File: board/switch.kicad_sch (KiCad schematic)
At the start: 2 parts

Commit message: Fix PCB problems
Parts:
- renumbered D_L_4_0 to D_L_4_2, SW_L_4_0 to SW_L_4_2
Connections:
- net ROW: now also D_L_4_2.1 (K); no longer D_L_4_2.2 (A)
- net at SW_L_4_2.5: now also D_L_4_2.2 (A); no longer D_L_4_2.1 (K)
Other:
- moved on the sheet: D_L_4_2

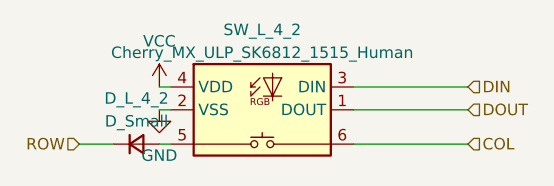
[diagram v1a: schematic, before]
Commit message: Switched to SMD switches
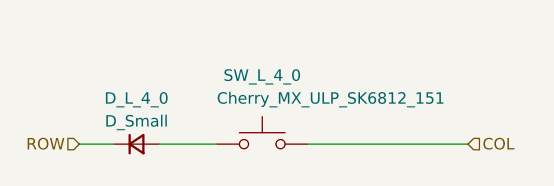
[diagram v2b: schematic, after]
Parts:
- D_L_4_0: renamed from D_L_4_2; LCSC (none) -> C2099
- SW_L_4_0: renamed from SW_L_4_2; value Cherry_MX_ULP_SK6812_1515_Human -> Cherry_MX_ULP_SK6812_151; footprint mnhttn:Cherry_MX_ULP_Human -> mnhttn:Cherry_MX_ULP; symbol mnhttn:Cherry_MX_ULP_SK6812_1515_Human -> Switch:SW_Push
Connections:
- net DOUT is gone; now on an unnamed net: SW_L_4_0.1
- net GND is gone; now on net COL: SW_L_4_0.2
- net COL: no longer SW_L_4_0.6
- net at D_L_4_0.2 (A): no longer SW_L_4_0.5
- removed net DIN: SW_L_4_0.3 (DIN)
- removed net VCC: SW_L_4_0.4 (VDD)

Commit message: Add battery connector
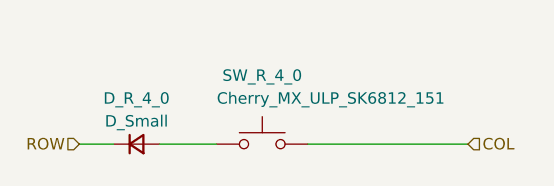
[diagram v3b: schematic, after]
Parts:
- renumbered D_L_4_0 to D_R_4_0, SW_L_4_0 to SW_R_4_0
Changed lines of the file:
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@@
 (kicad_sch
-	(version 20231120)
+	(version 20250114)
 	(generator "eeschema")
-	(generator_version "8.0")
+	(generator_version "9.0")
 	(paper "A4")
 	(wire
@@
 		(shape input)
 		(at 118.11 106.68 180)
-		(fields_autoplaced yes)
 		(effects
 			(font
@@
 		(shape input)
 		(at 161.29 106.68 0)
-		(fields_autoplaced yes)
 		(effects
 			(font
@@
 		(dnp no)
 		(fields_autoplaced yes)
-		(property "Reference" "D_L_4_0"
+		(property "Reference" "D_R_4_0"
 			(at 124.46 101.6 0)
 			(effects
@@
 		(on_board yes)
 		(dnp no)
-		(property "Reference" "SW_L_4_0"
+		(property "Reference" "SW_R_4_0"
 			(at 138.43 99.06 0)
 			(effects

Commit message: SMD only, On/Off symbole, Cleanup
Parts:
- D_R_4_0: Digikey (none) -> 1655-1N4148WTR-ND; LCSC C2099 -> (none)
- SW_R_4_0: Digikey (none) -> MX6C-K3NB
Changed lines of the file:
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@@
 (kicad_sch
-	(version 20250114)
+	(version 20260306)
 	(generator "eeschema")
-	(generator_version "9.0")
+	(generator_version "10.0")
 	(paper "A4")
 	(wire
@@
 		(at 124.46 106.68 0)
 		(unit 1)
+		(body_style 1)
 		(exclude_from_sim no)
 		(in_bom yes)
 		(on_board yes)
+		(in_pos_files yes)
 		(dnp no)
 		(fields_autoplaced yes)
 		(property "Reference" "D_R_4_0"
 			(at 124.46 101.6 0)
+			(show_name no)
+			(do_not_autoplace no)
 			(effects
 				(font
@@
 		(property "Value" "D_Small"
 			(at 124.46 104.14 0)
+			(show_name no)
+			(do_not_autoplace no)
 			(effects
 				(font
@@
 		(property "Footprint" "mnhttn:Diode_SOD123"
 			(at 124.46 106.68 90)
-			(effects
-				(font
-					(size 1.27 1.27)
-				)
-				(hide yes)
-			)
-		)
-		(property "Datasheet" "~"
+			(hide yes)
+			(show_name no)
+			(do_not_autoplace no)
+			(effects
+				(font
+					(size 1.27 1.27)
+				)
+			)
+		)
+		(property "Datasheet" ""
 			(at 124.46 106.68 90)
-			(effects
-				(font
-					(size 1.27 1.27)
-				)
-				(hide yes)
+			(hide yes)
+			(show_name no)
+			(do_not_autoplace no)
+			(effects
+				(font
+					(size 1.27 1.27)
+				)
 			)
 		)
 		(property "Description" ""
 			(at 124.46 106.68 0)
-			(effects
-				(font
-					(size 1.27 1.27)
-				)
-				(hide yes)
-			)
-		)
-		(property "LCSC" "C2099"
+			(hide yes)
+			(show_name no)
+			(do_not_autoplace no)
+			(effects
+				(font
+					(size 1.27 1.27)
+				)
+			)
+		)
+		(property "Digikey" "1655-1N4148WTR-ND"
 			(at 124.46 106.68 0)
-			(effects
-				(font
-					(size 1.27 1.27)
-				)
-				(hide yes)
+			(hide yes)
+			(show_name no)
+			(do_not_autoplace no)
+			(effects
+				(font
+					(size 1.27 1.27)
+				)
 			)
 		)
@@
 		(at 138.43 106.68 0)
 		(unit 1)
+		(body_style 1)
 		(exclude_from_sim no)
 		(in_bom yes)
 		(on_board yes)
+		(in_pos_files yes)
 		(dnp no)
 		(property "Reference" "SW_R_4_0"
 			(at 138.43 99.06 0)
+			(show_name no)
+			(do_not_autoplace no)
 			(effects
 				(font
@@
 		(property "Value" "Cherry_MX_ULP_SK6812_151"
 			(at 146.05 101.6 0)
+			(show_name no)
+			(do_not_autoplace no)
 			(effects
 				(font
@@
 		(property "Footprint" "mnhttn:Cherry_MX_ULP"
 			(at 138.43 101.6 0)
-			(effects
-				(font
-					(size 1.27 1.27)
-				)
-				(hide yes)
-			)
-		)
-		(property "Datasheet" "~"
+			(hide yes)
+			(show_name no)
+			(do_not_autoplace no)
+			(effects
+				(font
+					(size 1.27 1.27)
+				)
+			)
+		)
+		(property "Datasheet" ""
 			(at 138.43 101.6 0)
-			(effects
-				(font
-					(size 1.27 1.27)
-				)
-				(hide yes)
+			(hide yes)
+			(show_name no)
+			(do_not_autoplace no)
+			(effects
+				(font
+					(size 1.27 1.27)
+				)
 			)
 		)
 		(property "Description" "Push button switch, generic, two pins"
 			(at 138.43 106.68 0)
-			(effects
-				(font
-					(size 1.27 1.27)
-				)
-				(hide yes)
-			)
-		)
+			(hide yes)
+			(show_name no)
+			(do_not_autoplace no)
+			(effects
+				(font
+					(size 1.27 1.27)
+				)
+			)
+		)
+		(property "Digikey" "MX6C-K3NB"
+			(at 138.43 106.68 0)
+			(hide yes)
+			(show_name no)
+			(do_not_autoplace no)
+			(effects
+				(font
+					(size 1.27 1.27)
+				)
+			)
+		)
